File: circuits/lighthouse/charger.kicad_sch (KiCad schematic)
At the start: 15 parts, among them J1 USB_C_Receptacle_PowerOnly_6P, Q2 FS8205A, U4 TP4056-42-ESOP8, U5 DW01A

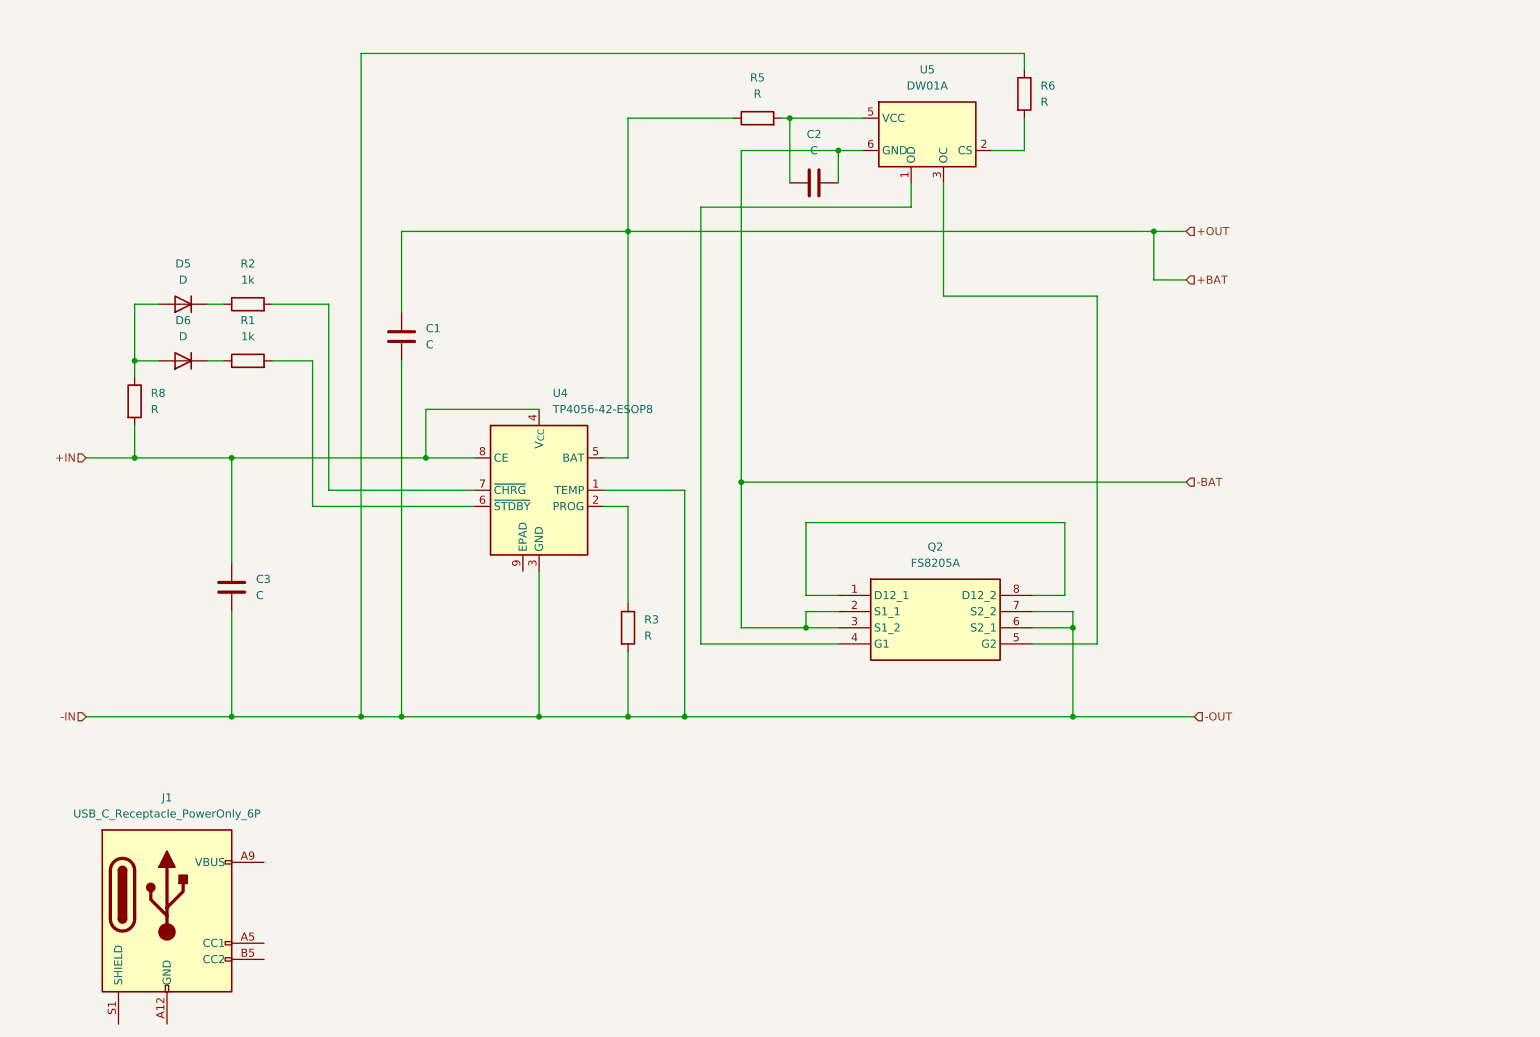
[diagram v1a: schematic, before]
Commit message: The circuit now has all the values in place
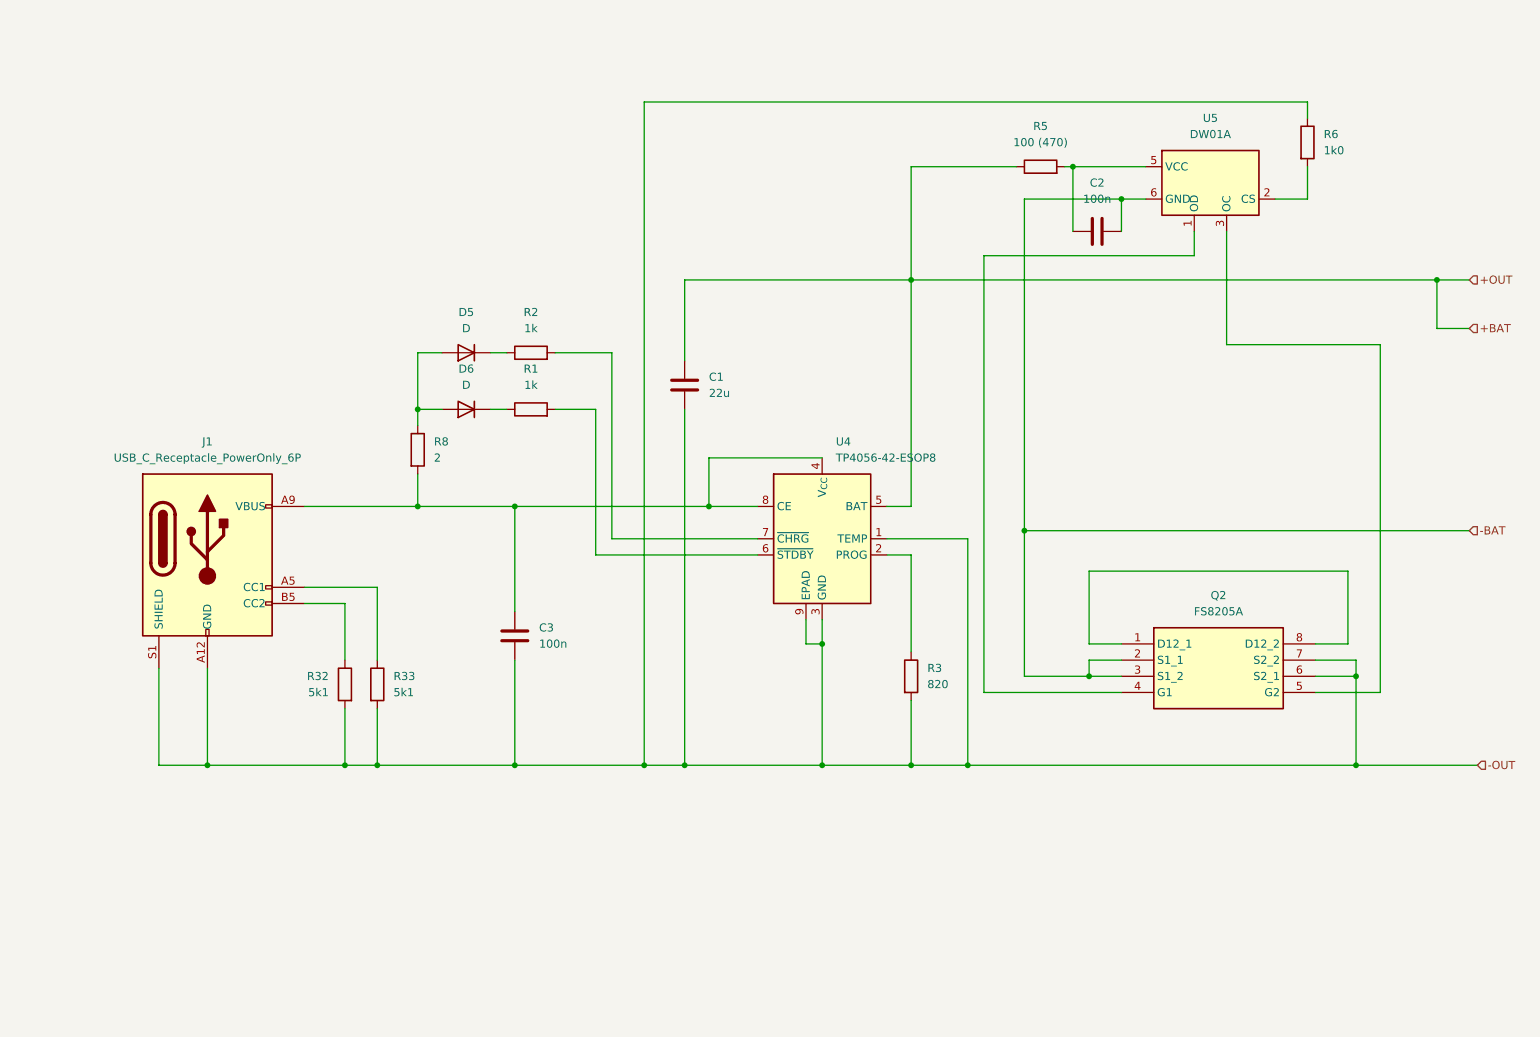
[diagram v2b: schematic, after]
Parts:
- added R32, R33: 5k1, Resistor_SMD:R_1206_3216Metric_Pad1.30x1.75mm_HandSolder, symbol Device:R
- C1: value C -> 22u
- C2, C3: value C -> 100n
- J1: footprint (none) -> Connector_USB:USB_C_Receptacle_GCT_USB4125-xx-x_6P_TopMnt_Horizontal
- R3: value R -> 820
- R5: value R -> 100 (470)
- R6: value R -> 1k0
- R8: value R -> 2
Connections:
- net +IN is gone; now on an unnamed net: C3.1, R8.2, U4.4 (V_{CC}), U4.8 (CE)
- net -IN is gone; now on net -OUT: C1.2, C3.2, Q2.6 (S2_1), Q2.7 (S2_2), R3.2, R6.1, U4.1 (TEMP), U4.3 (GND)
- net -OUT: now reaches J1.A12 (GND), J1.B12 (GND)
- net -OUT: now also J1.S1 (SHIELD), U4.9 (EPAD), R32.2, R33.2
- net at J1.A5 (CC1): now also R33.1
- net at J1.B5 (CC2): now also R32.1
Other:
- moved on the sheet: C1, C2, C3, D5, D6, J1, Q2, R1, R2, R3, R5, R6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

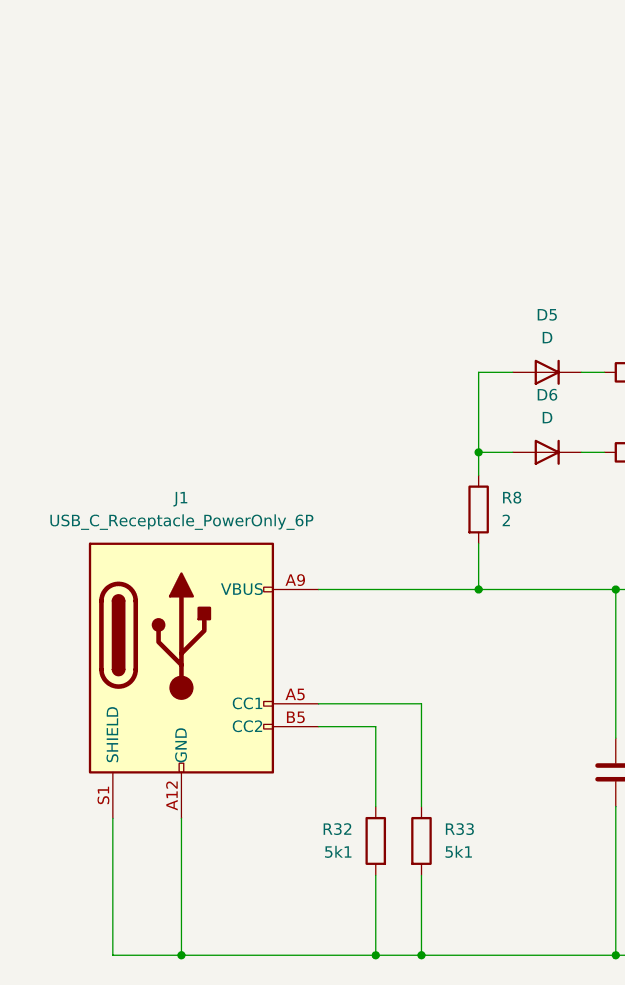
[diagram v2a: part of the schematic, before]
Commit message: Removed one connector from the schematic
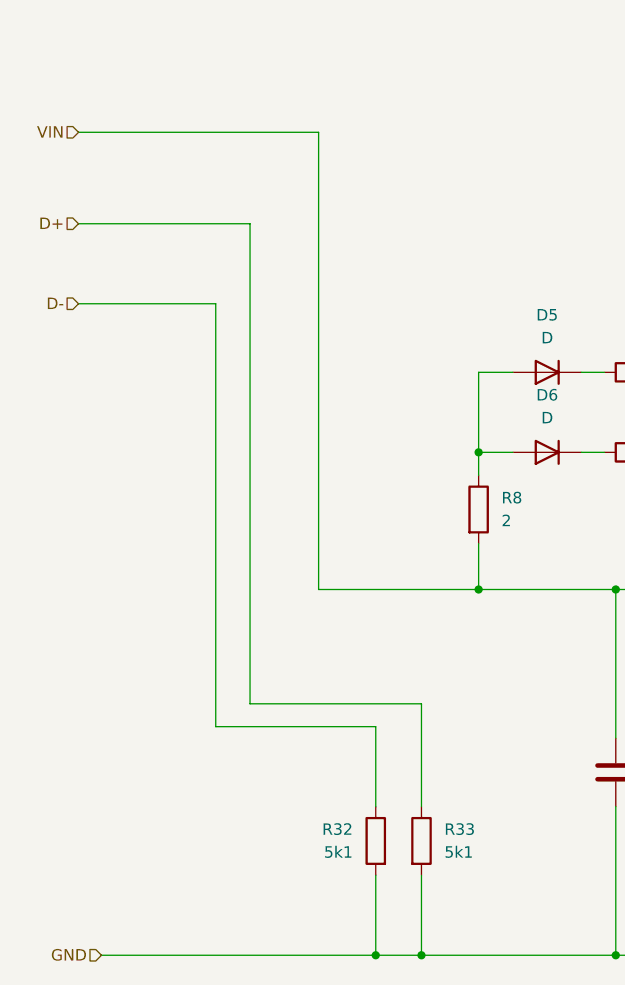
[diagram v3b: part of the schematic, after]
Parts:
- removed J1: USB_C_Receptacle_PowerOnly_6P, Connector_USB:USB_C_Receptacle_GCT_USB4125-xx-x_6P_TopMnt_Horizontal, symbol Connector:USB_C_Receptacle_PowerOnly_6P
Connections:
- net D+: now reaches R33.1
- net VIN: now reaches C3.1, R8.2, U4.4 (V_{CC}), U4.8 (CE)
- net D-: now reaches R32.1
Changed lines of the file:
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@@
-	)
-	(junction
-		(at 48.26 139.7)
-		(diameter 0)
-		(color 0 0 0 0)
 	)
 	(junction
@@
 	(wire
 		(pts
-			(xy 69.85 114.3) (xy 63.5 114.3)
-		)
-		(stroke
-			(width 0)
-			(type default)
-		)
-	)
-	(wire
-		(pts
 			(xy 85.09 74.93) (xy 81.28 74.93)
 		)
@@
 	(wire
 		(pts
-			(xy 48.26 139.7) (xy 69.85 139.7)
-		)
-		(stroke
-			(width 0)
-			(type default)
-		)
-	)
-	(wire
-		(pts
 			(xy 228.6 139.7) (xy 247.65 139.7)
 		)
@@
 	(wire
 		(pts
-			(xy 63.5 111.76) (xy 74.93 111.76)
+			(xy 39.37 139.7) (xy 69.85 139.7)
 		)
 		(stroke
@@
 	(wire
 		(pts
+			(xy 52.07 114.3) (xy 52.07 67.31)
+		)
+		(stroke
+			(width 0)
+			(type default)
+		)
+	)
+	(wire
+		(pts
 			(xy 154.94 106.68) (xy 158.75 106.68)
 		)
@@
 	(wire
 		(pts
-			(xy 40.64 124.46) (xy 40.64 139.7)
-		)
-		(stroke
-			(width 0)
-			(type default)
-		)
-	)
-	(wire
-		(pts
 			(xy 158.75 99.06) (xy 158.75 63.5)
 		)
@@
 	(wire
 		(pts
+			(xy 63.5 99.06) (xy 63.5 48.26)
+		)
+		(stroke
+			(width 0)
+			(type default)
+		)
+	)
+	(wire
+		(pts
 			(xy 191.77 128.27) (xy 170.18 128.27)
 		)
@@
 	(wire
 		(pts
+			(xy 55.88 111.76) (xy 55.88 58.42)
+		)
+		(stroke
+			(width 0)
+			(type default)
+		)
+	)
+	(wire
+		(pts
 			(xy 176.53 50.8) (xy 176.53 102.87)
 		)
@@
 	(wire
 		(pts
+			(xy 55.88 111.76) (xy 74.93 111.76)
+		)
+		(stroke
+			(width 0)
+			(type default)
+		)
+	)
+	(wire
+		(pts
 			(xy 154.94 99.06) (xy 158.75 99.06)
 		)
@@
 	(wire
 		(pts
-			(xy 40.64 139.7) (xy 48.26 139.7)
-		)
-		(stroke
-			(width 0)
-			(type default)
-		)
-	)
-	(wire
-		(pts
-			(xy 48.26 124.46) (xy 48.26 139.7)
-		)
-		(stroke
-			(width 0)
-			(type default)
-		)
-	)
-	(wire
-		(pts
 			(xy 81.28 83.82) (xy 81.28 86.36)
 		)
@@
 	(wire
 		(pts
+			(xy 63.5 48.26) (xy 36.83 48.26)
+		)
+		(stroke
+			(width 0)
+			(type default)
+		)
+	)
+	(wire
+		(pts
 			(xy 96.52 115.57) (xy 96.52 99.06)
 		)
@@
 	(wire
 		(pts
+			(xy 52.07 114.3) (xy 69.85 114.3)
+		)
+		(stroke
+			(width 0)
+			(type default)
+		)
+	)
+	(wire
+		(pts
 			(xy 176.53 125.73) (xy 176.53 102.87)
 		)
@@
 	(wire
 		(pts
+			(xy 52.07 67.31) (xy 36.83 67.31)
+		)
+		(stroke
+			(width 0)
+			(type default)
+		)
+	)
+	(wire
+		(pts
 			(xy 208.28 73.66) (xy 232.41 73.66)
 		)
@@
 	(wire
 		(pts
+			(xy 55.88 58.42) (xy 36.83 58.42)
+		)
+		(stroke
+			(width 0)
+			(type default)
+		)
+	)
+	(wire
+		(pts
 			(xy 222.25 123.19) (xy 228.6 123.19)
 		)
@@
 			(width 0)
 			(type default)
+		)
+	)
+	(hierarchical_label "D-"
+		(shape input)
+		(at 36.83 67.31 180)
+		(effects
+			(font
+				(size 1.27 1.27)
+			)
+			(justify right)
 		)
 	)
@@
 		)
 	)
+	(hierarchical_label "VIN"
+		(shape input)
+		(at 36.83 48.26 180)
+		(effects
+			(font
+				(size 1.27 1.27)
+			)
+			(justify right)
+		)
+	)
 	(hierarchical_label "-OUT"
 		(shape input)
@@
 			)
 			(justify left)
+		)
+	)
+	(hierarchical_label "D+"
+		(shape input)
+		(at 36.83 58.42 180)
+		(effects
+			(font
+				(size 1.27 1.27)
+			)
+			(justify right)
+		)
+	)
+	(hierarchical_label "GND"
+		(shape input)
+		(at 39.37 139.7 180)
+		(effects
+			(font
+				(size 1.27 1.27)
+			)
+			(justify right)
 		)
 	)
@@
 					(unit 1)
 				)
-			)
-		)
-	)
-	(symbol
-		(lib_id "Connector:USB_C_Receptacle_PowerOnly_6P")
-		(at 48.26 106.68 0)
-		(unit 1)
-		(exclude_from_sim no)
-		(in_bom yes)
-		(on_board yes)
-		(dnp no)
-		(fields_autoplaced yes)
-		(property "Reference" "J1"
-			(at 48.26 88.9 0)
-			(effects
-				(font
-					(size 1.27 1.27)
-				)
-			)
-		)
-		(property "Value" "USB_C_Receptacle_PowerOnly_6P"
-			(at 48.26 91.44 0)
-			(effects
-				(font
-					(size 1.27 1.27)
-				)
-			)
-		)
-		(property "Footprint" "Connector_USB:USB_C_Receptacle_GCT_USB4125-xx-x_6P_TopMnt_Horizontal"
-			(at 52.07 104.14 0)
-			(effects
-				(font
-					(size 1.27 1.27)
-				)
-				(hide yes)
-			)
-		)
-		(property "Datasheet" "https://www.usb.org/sites/default/files/documents/usb_type-c.zip"
-			(at 48.26 106.68 0)
-			(effects
-				(font
-					(size 1.27 1.27)
-				)
-				(hide yes)
-			)
-		)
-		(property "Description" "USB Power-Only 6P Type-C Receptacle connector"
-			(at 48.26 106.68 0)
-			(effects
-				(font
-					(size 1.27 1.27)
-				)
-				(hide yes)
-			)
-		)
-		(pin "A5"
-		)
-		(pin "A12"
-		)
-		(pin "B12"
-		)
-		(pin "A9"
-		)
-		(pin "B5"
-		)
-		(pin "B9"
-		)
-		(pin "S1"
-		)
-		(instances
-			(project "lighthouse"
-				(path "/7210d03b-7565-45ff-aaca-ad566f37cd67/adf63908-e234-4fc5-b1bf-4049b839acc1"
-					(reference "J1")
-					(unit 1)
-				)

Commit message: Rewamped the pcb
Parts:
- removed R8: 2, Resistor_SMD:R_1206_3216Metric_Pad1.30x1.75mm_HandSolder, symbol Device:R
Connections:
- net VIN: now also D5.2 (A), D6.2 (A)
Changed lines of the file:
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@@
-	(wire
-		(pts
-			(xy 81.28 83.82) (xy 81.28 86.36)
-		)
-		(stroke
-			(width 0)
-			(type default)
-		)
-	)
 	(wire
 		(pts
@@
 	(wire
 		(pts
-			(xy 81.28 93.98) (xy 81.28 99.06)
+			(xy 81.28 83.82) (xy 81.28 99.06)
 		)
 		(stroke
@@
 					(unit 1)
 				)
-			)
-		)
-	)
-	(symbol
-		(lib_id "Device:R")
-		(at 81.28 90.17 0)
-		(unit 1)
-		(exclude_from_sim no)
-		(in_bom yes)
-		(on_board yes)
-		(dnp no)
-		(fields_autoplaced yes)
-		(property "Reference" "R8"
-			(at 83.82 88.8999 0)
-			(effects
-				(font
-					(size 1.27 1.27)
-				)
-				(justify left)
-			)
-		)
-		(property "Value" "2"
-			(at 83.82 91.4399 0)
-			(effects
-				(font
-					(size 1.27 1.27)
-				)
-				(justify left)
-			)
-		)
-		(property "Footprint" "Resistor_SMD:R_1206_3216Metric_Pad1.30x1.75mm_HandSolder"
-			(at 79.502 90.17 90)
-			(effects
-				(font
-					(size 1.27 1.27)
-				)
-				(hide yes)
-			)
-		)
-		(property "Datasheet" "~"
-			(at 81.28 90.17 0)
-			(effects
-				(font
-					(size 1.27 1.27)
-				)
-				(hide yes)
-			)
-		)
-		(property "Description" "Resistor"
-			(at 81.28 90.17 0)
-			(effects
-				(font
-					(size 1.27 1.27)
-				)
-				(hide yes)
-			)
-		)
-		(pin "2"
-		)
-		(pin "1"
-		)
-		(instances
-			(project "lighthouse"
-				(path "/7210d03b-7565-45ff-aaca-ad566f37cd67/adf63908-e234-4fc5-b1bf-4049b839acc1"
-					(reference "R8")
-					(unit 1)
-				)

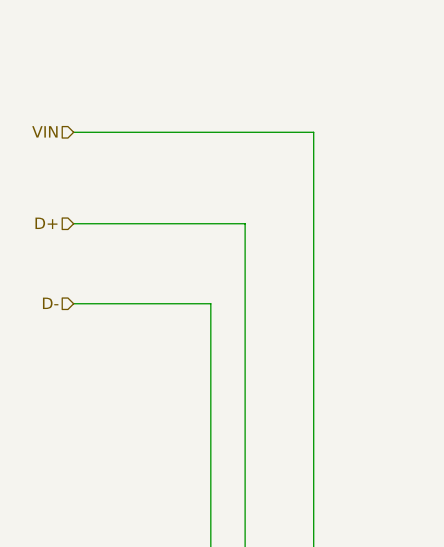
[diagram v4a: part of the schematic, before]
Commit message: Changed to a correct usb C port
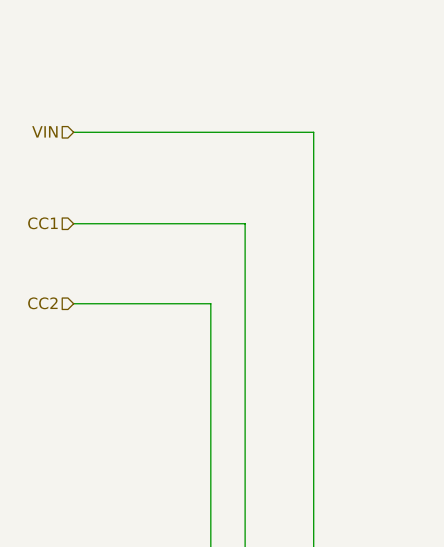
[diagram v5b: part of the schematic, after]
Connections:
- net D+ renamed CC1
- net D- renamed CC2
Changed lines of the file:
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@@
 		)
 	)
-	(hierarchical_label "D-"
+	(hierarchical_label "CC2"
 		(shape input)
 		(at 36.83 67.31 180)
@@
 		)
 	)
-	(hierarchical_label "D+"
+	(hierarchical_label "CC1"
 		(shape input)
 		(at 36.83 58.42 180)

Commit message: Cleaned up schematics
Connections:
- net +BAT: now also R5.2; no longer R5.1
- net -OUT: now also Q2.5 (G2), R6.2, U5.3 (OC); no longer R6.1
- net at C2.1, U5.5 (VCC): now also R5.1; no longer R5.2
- net at U5.2 (CS): now also R6.1; no longer R6.2
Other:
- moved on the sheet: C1, C2, C3, D5, D6, Q2, R1, R2, R3, R32, R33, R5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

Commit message: Sorted out pcb layers
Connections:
- net +BAT: now also R5.1; no longer R5.2
- net -OUT: now also R6.1; no longer Q2.5 (G2), R6.2, U5.3 (OC)
- net at C2.1, U5.5 (VCC): now also R5.2; no longer R5.1
- net at U5.2 (CS): now also R6.2; no longer R6.1
- new net: Q2.5 (G2), U5.3 (OC)
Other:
- moved on the sheet: C1, C2, C3, D5, D6, Q2, R1, R2, R3, R32, R33, R5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

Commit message: Production ready board
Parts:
- removed D5, D6: D, LED_SMD:LED_1206_3216Metric_Pad1.42x1.75mm_HandSolder, symbol Device:D
- removed R32, R33: 5k1, Resistor_SMD:R_1206_3216Metric_Pad1.30x1.75mm_HandSolder, symbol Device:R
- added D5, D6: LED, LED_SMD:LED_1206_3216Metric_Pad1.42x1.75mm_HandSolder, symbol Device:LED
- R3: value 820 -> 1k
- R5: value 100 (470) -> 150
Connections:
- net VIN: now also D5.2 (A), D6.2 (A)
- net at R1.1: now also D6.1 (K)
- net at R2.1: now also D5.1 (K)
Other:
- moved on the sheet: C1, C2, C3, Q2, R1, R2, R3, R5, R6, U4, U5
